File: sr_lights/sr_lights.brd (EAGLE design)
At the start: 78.4 x 64.8 mm, 33 parts, among them T1 BC847, T2 BC847, T3 BC847, T4 BC847, T5 BC847, T6 BC847, T7 BC847, T8 BC847

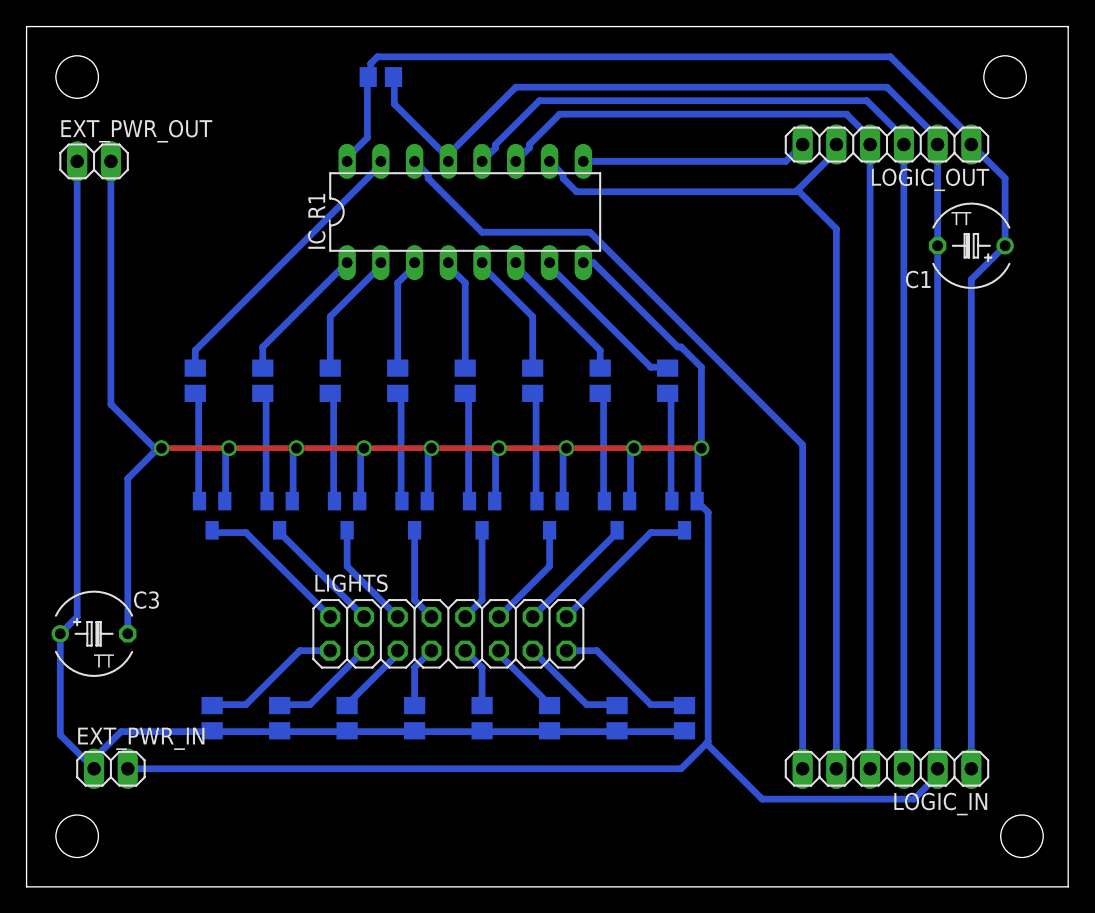
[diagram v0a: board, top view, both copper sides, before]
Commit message: Minor changes in sr_lights: DRC check, GND plane, moved some routes and components
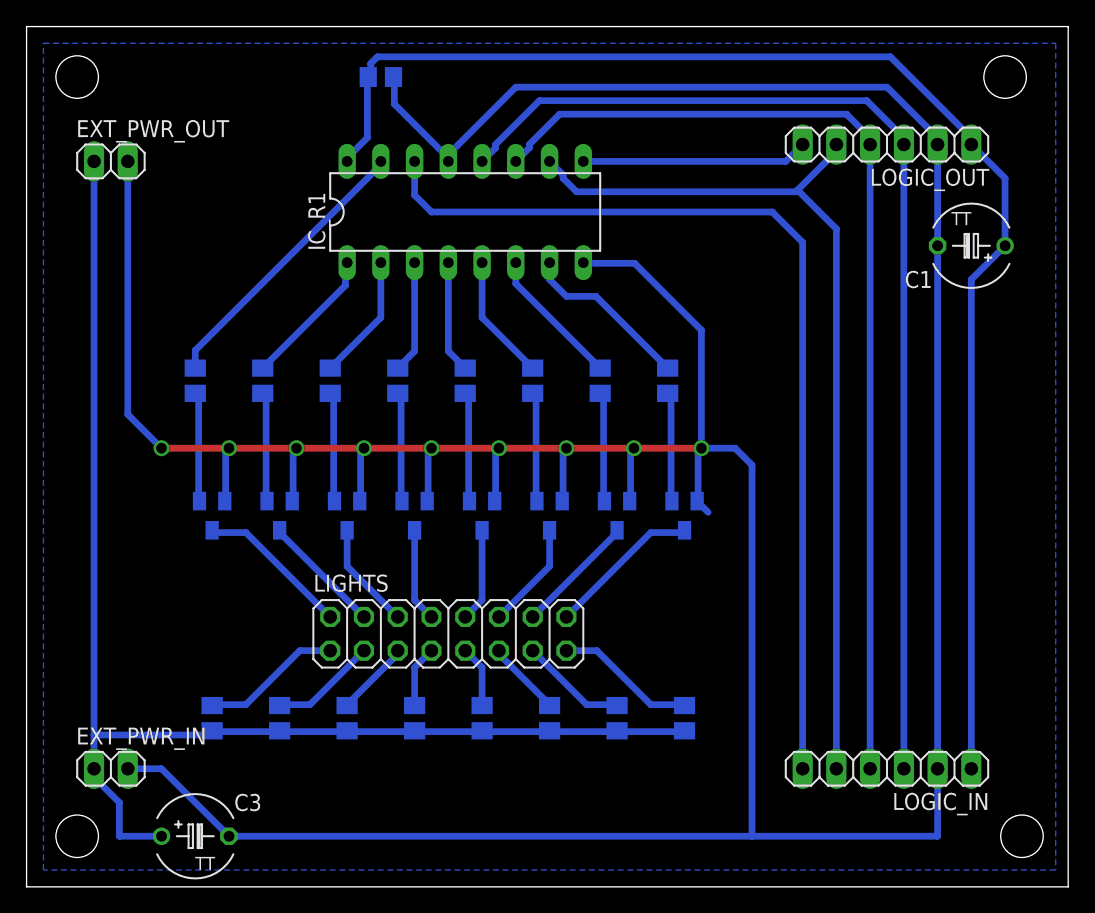
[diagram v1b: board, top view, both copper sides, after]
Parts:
- moved C3 17.0 mm to (12.7, 3.81)
- moved EXT_PWR_OUT 1.27 mm to (6.35, 54.6)
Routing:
- net SI0: track 62.6 -> 72.8 mm
- net VCC2: track 94.0 -> 100.1 mm
- net GND: track 310.7 -> 314.3 mm
- added copper zone on layer 16, net GND
